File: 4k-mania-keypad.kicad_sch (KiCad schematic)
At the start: 49 parts, among them J1 USB_C_Receptacle_USB2.0, J4 Conn_01x03, J5 Conn_01x03, J6 Conn_01x03, J7 Conn_01x03, SW1 RotaryEncoder_Switch, SW2 RotaryEncoder_Switch, SW3 SW_Push, U1 AP2112K-3.3, U2 RP2040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

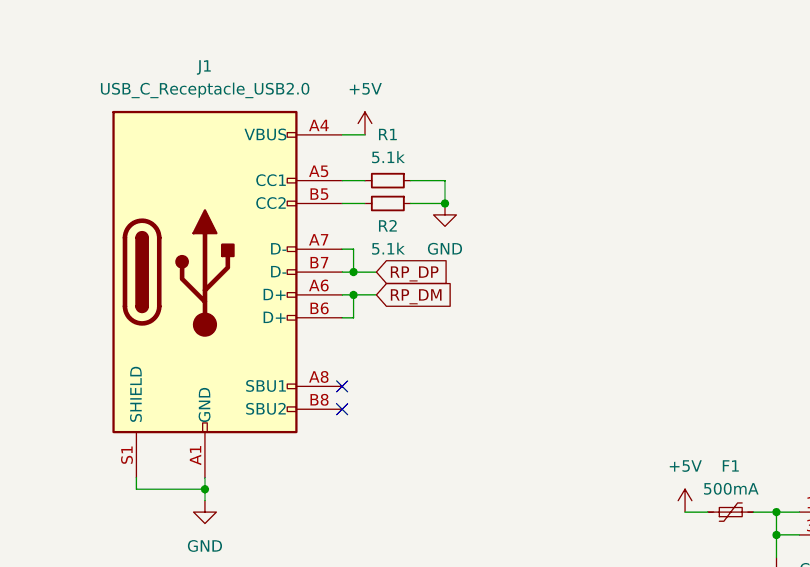
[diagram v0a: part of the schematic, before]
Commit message: usb routing fix
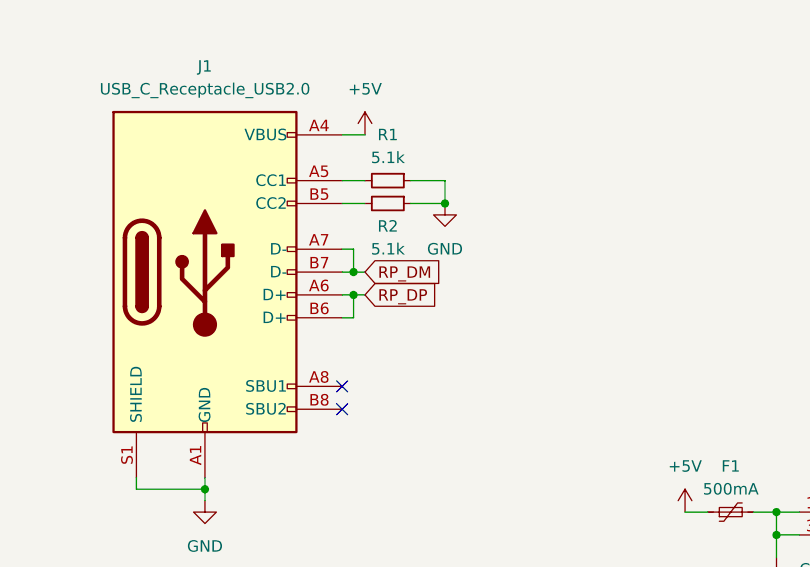
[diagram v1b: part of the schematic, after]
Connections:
- net RP_DM: now also J1.A7 (D-), J1.B7 (D-); no longer J1.A6 (D+), J1.B6 (D+)
- net RP_DP: now also J1.A6 (D+), J1.B6 (D+); no longer J1.A7 (D-), J1.B7 (D-)
